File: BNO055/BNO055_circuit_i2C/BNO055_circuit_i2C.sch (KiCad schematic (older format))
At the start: 11 parts, among them U1 BNO055

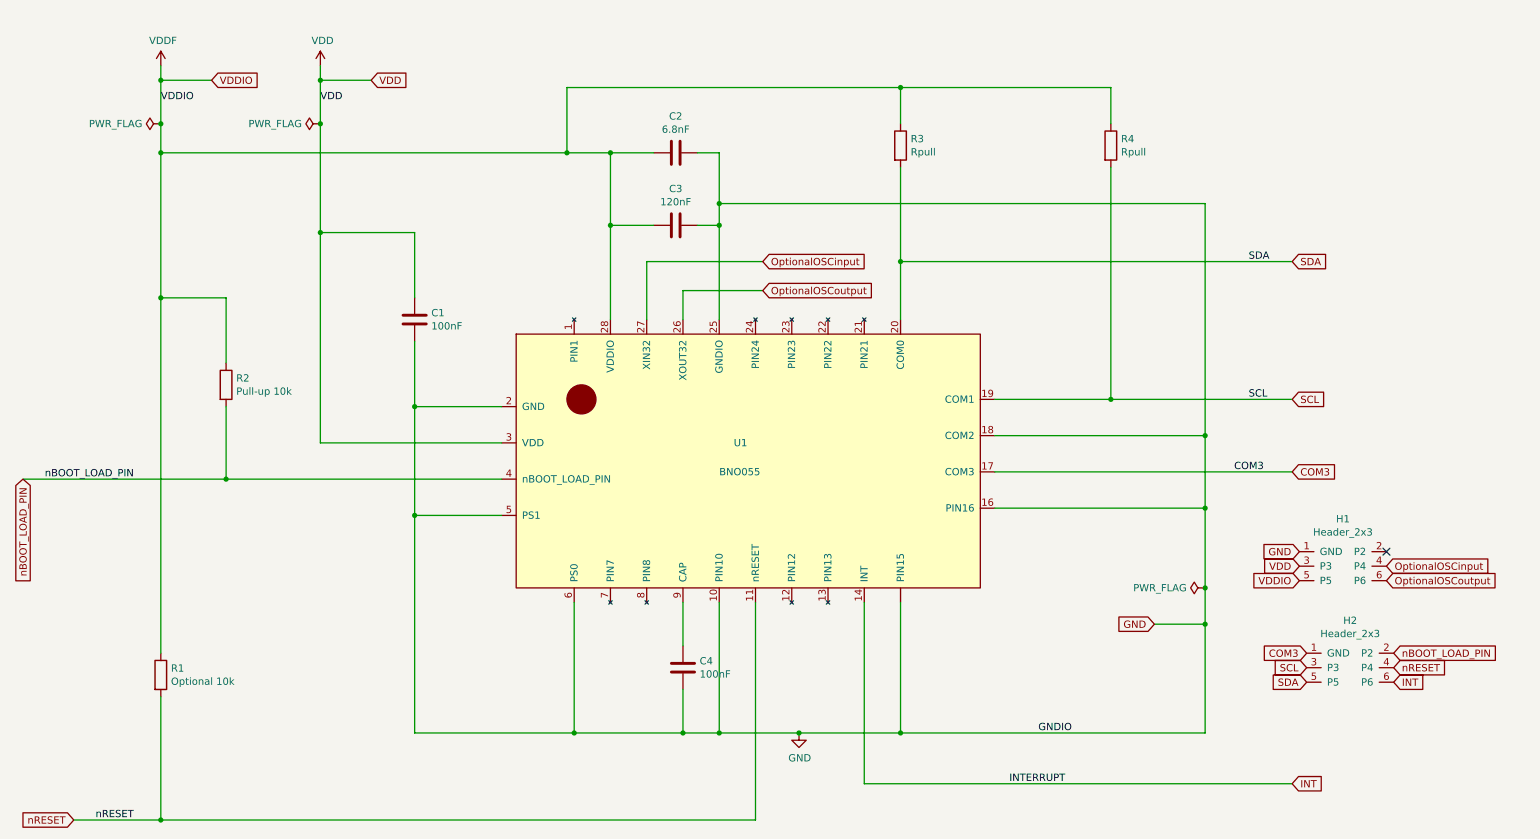
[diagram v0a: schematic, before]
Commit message: redesign BNO055 breakout, except for small changes
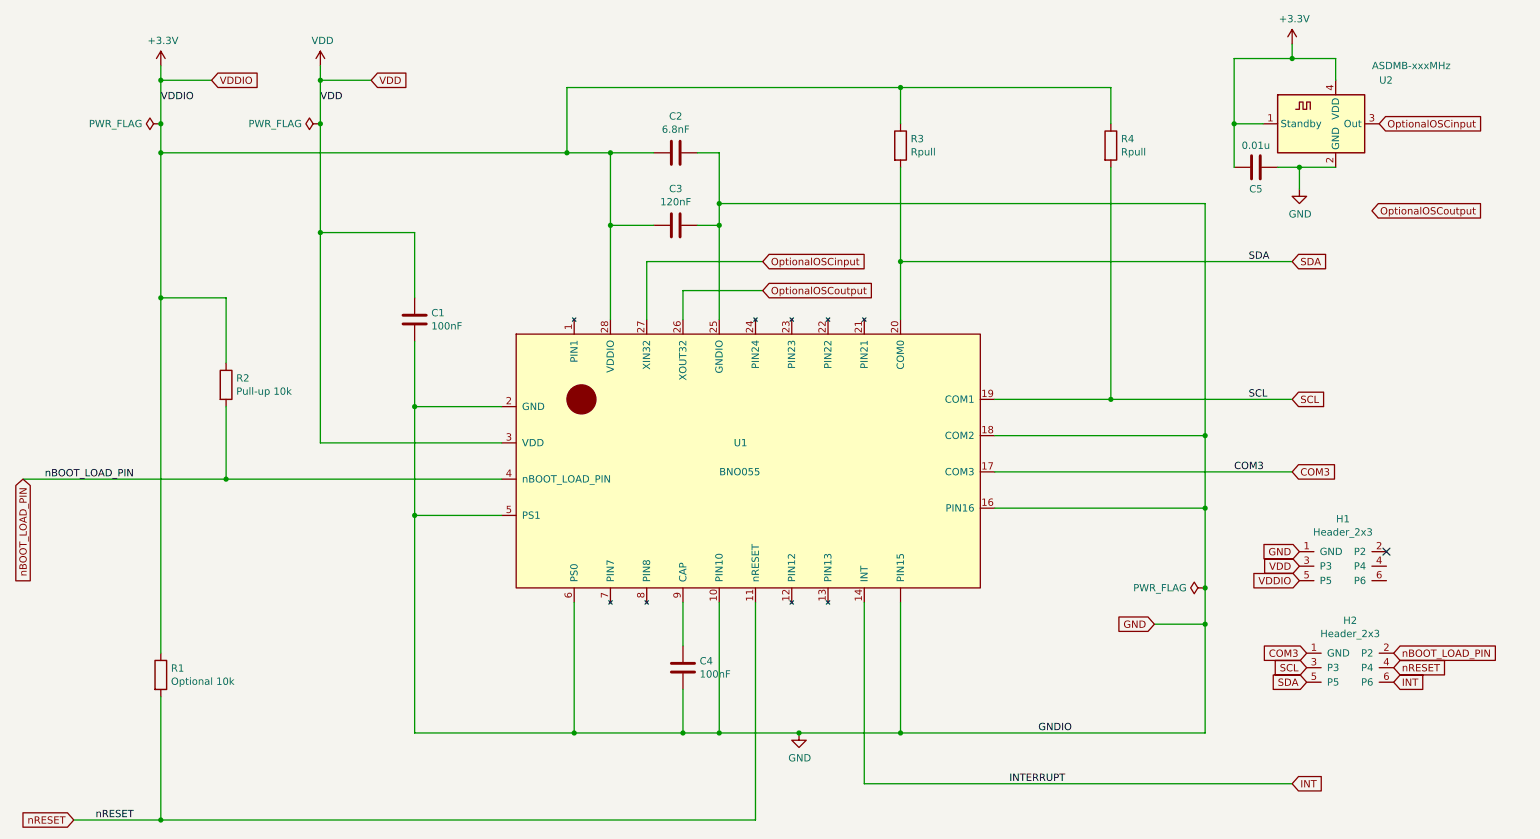
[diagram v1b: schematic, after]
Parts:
- added C5: 0.01u, footprints:C_0603_1608Metric, symbol Device:C
- added U2: ASDMB-xxxMHz, ASDK2-32.768KHZ-LR-T3:ASDK2-32.768KHZ-LR-T3, symbol Oscillator:ASDMB-xxxMHz
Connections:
- net GND: now also C5.1, U2.2 (GND)
- net OptionalOSCinput: now also U2.3 (Out); no longer H1.4 (P4)
- net OptionalOSCoutput: no longer H1.6 (P6)
- net VDDF renamed +3V3
- net +3V3: now also C5.2, U2.1 (Standby), U2.4 (VDD)
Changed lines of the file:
@@
 	1    0    0    -1
 $EndComp
-$Comp
-L power:VDDF #PWR0103
-U 1 1 5F89F746
-P 1900 1150
-F 0 "#PWR0103" H 1900 1000 50  0001 C CNN
-F 1 "VDDF" H 1915 1323 50  0000 C CNN
-F 2 "" H 1900 1150 50  0001 C CNN
-F 3 "" H 1900 1150 50  0001 C CNN
-	1    1900 1150
-	1    0    0    -1
-$EndComp
-Wire Wire Line
-	3650 3500 3650 4250
 Wire Wire Line
 	1900 1750 1900 1550
@@
 Text Label 1100 4000 0    50   ~ 0
 nBOOT_LOAD_PIN
-Text GLabel 10350 4600 2    50   Input ~ 0
-OptionalOSCinput
-Text GLabel 10350 4700 2    50   Input ~ 0
+Text GLabel 10250 2150 2    50   Input ~ 0
 OptionalOSCoutput
 Connection ~ 7000 2500
@@
 Wire Wire Line
 	5750 2100 9100 2100
-Connection ~ 3650 4250
-Wire Wire Line
-	3650 4250 3650 5750
 Wire Wire Line
 	3650 3050 3650 3500
@@
 Wire Wire Line
 	4750 4850 4750 5750
-Wire Wire Line
-	4250 4250 3650 4250
 Wire Wire Line
 	4250 4000 2350 4000
@@
 $EndComp
 NoConn ~ 10350 4500
+$Comp
+L Oscillator:ASDMB-xxxMHz U2
+U 1 1 5FA4E8B7
+P 9900 1550
+F 0 "U2" H 10300 1850 50  0000 L CNN
+F 1 "ASDMB-xxxMHz" H 10250 1950 50  0000 L CNN
+F 2 "ASDK2-32.768KHZ-LR-T3:ASDK2-32.768KHZ-LR-T3" H 9900 1550 50  0001 C CNN
+F 3 "https://abracon.com/Oscillators/ASDK.pdf" H 10200 2000 50  0001 C CNN
+	1    9900 1550
+	1    0    0    -1
+$EndComp
+Text GLabel 10300 1550 2    50   Input ~ 0
+OptionalOSCinput
+Wire Wire Line
+	10000 1250 10000 1100
+Wire Wire Line
+	10000 1100 9700 1100
+Wire Wire Line
+	9300 1100 9300 1550
+Wire Wire Line
+	9300 1550 9500 1550
+$Comp
+L power:+3.3V #PWR01
+U 1 1 5FA58E82
+P 1900 1150
+F 0 "#PWR01" H 1900 1000 50  0001 C CNN
+F 1 "+3.3V" H 1915 1323 50  0000 C CNN
+F 2 "" H 1900 1150 50  0001 C CNN
+F 3 "" H 1900 1150 50  0001 C CNN
+	1    1900 1150
+	1    0    0    -1
+$EndComp
+$Comp
+L power:+3.3V #PWR02
+U 1 1 5FA5A832
+P 9700 1000
+F 0 "#PWR02" H 9700 850 50  0001 C CNN
+F 1 "+3.3V" H 9715 1173 50  0000 C CNN
+F 2 "" H 9700 1000 50  0001 C CNN
+F 3 "" H 9700 1000 50  0001 C CNN
+	1    9700 1000
+	1    0    0    -1
+$EndComp
+Wire Wire Line
+	9700 1000 9700 1100
+Connection ~ 9700 1100
+Wire Wire Line
+	9700 1100 9300 1100
+$Comp
+L power:GND #PWR03
+U 1 1 5FA5D601
+P 9750 2000
+F 0 "#PWR03" H 9750 1750 50  0001 C CNN
+F 1 "GND" H 9755 1827 50  0000 C CNN
+F 2 "" H 9750 2000 50  0001 C CNN
+F 3 "" H 9750 2000 50  0001 C CNN
+	1    9750 2000
+	1    0    0    -1
+$EndComp
+Wire Wire Line
+	10000 1850 9750 1850
+Wire Wire Line
+	9750 1850 9750 2000
+$Comp
+L Device:C C5
+U 1 1 5FA6257B
+P 9450 1850
+F 0 "C5" V 9600 1850 50  0000 C CNN
+F 1 "0.01u" V 9300 1850 50  0000 C CNN
+F 2 "footprints:C_0603_1608Metric" H 9488 1700 50  0001 C CNN
+F 3 "~" H 9450 1850 50  0001 C CNN
+	1    9450 1850
+	0    1    1    0
+$EndComp
+Wire Wire Line
+	9600 1850 9750 1850
+Connection ~ 9750 1850
+Wire Wire Line
+	9300 1850 9300 1550
+Connection ~ 9300 1550
+Wire Wire Line
+	3650 3500 3650 4250
+Wire Wire Line
+	4250 4250 3650 4250
+Connection ~ 3650 4250
+Wire Wire Line
+	3650 4250 3650 5750
 $EndSCHEMATC

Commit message: add MPL3115 barometer schematic and layout
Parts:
- H1, H2: symbol Olin_Rocketry_Symbols:Header_2x3 -> BNO055_circuit_i2C-rescue:Header_2x3-Olin_Rocketry_Symbols
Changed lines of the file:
@@
 nBOOT_LOAD_PIN
 $Comp
-L Olin_Rocketry_Symbols:Header_2x3 H1
+L BNO055_circuit_i2C-rescue:Header_2x3-Olin_Rocketry_Symbols H1
 U 1 1 5F967336
 P 10050 4600
@@
 $EndComp
 $Comp
-L Olin_Rocketry_Symbols:Header_2x3 H2
+L BNO055_circuit_i2C-rescue:Header_2x3-Olin_Rocketry_Symbols H2
 U 1 1 5F967DE8
 P 10100 5300
